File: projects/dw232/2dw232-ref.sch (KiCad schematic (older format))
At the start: 24 parts, among them P501 CONN_01X07, Q501 MMBT3904, Q502 MMBT3904, U501 LM741, U502 LM741, U503 2DW232

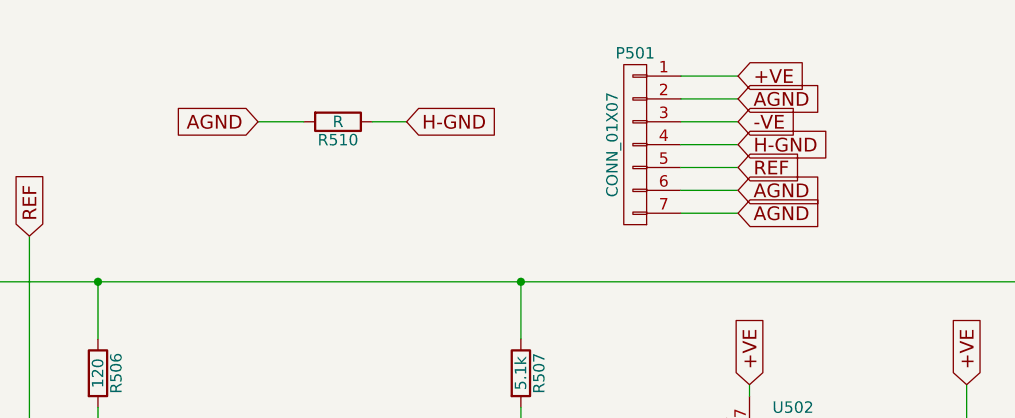
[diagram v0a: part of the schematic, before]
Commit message: remove old stuff for reference
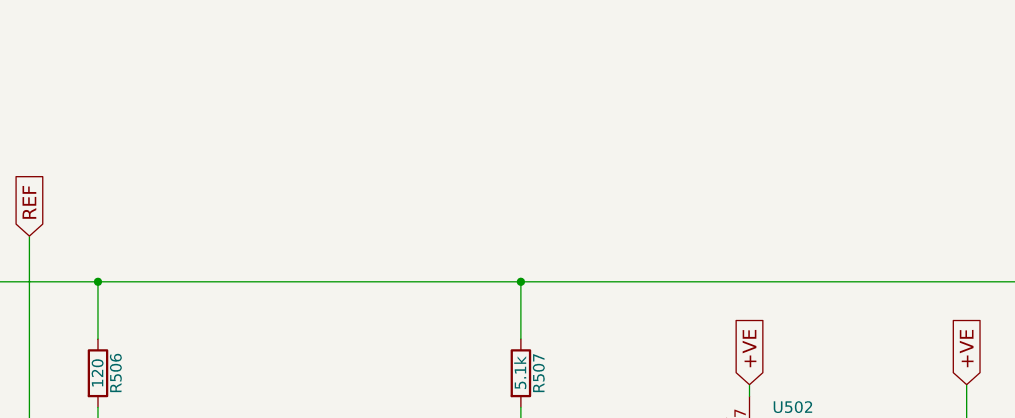
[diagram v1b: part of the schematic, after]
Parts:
- removed P501: CONN_01X07, Pin_Headers:Pin_Header_Straight_1x07, symbol CONN_01X07
- removed R510: R, Resistors_SMD:R_1206, symbol R
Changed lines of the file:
@@
 $Descr A4 11693 8268
 encoding utf-8
-Sheet 2 4
+Sheet 2 2
 Title ""
 Date ""
@@
 	1850 1400 1850 1600
 $Comp
-L CONN_01X07 P501
-U 1 1 5883052B
-P 6800 1150
-F 0 "P501" H 6800 1550 50  0000 C CNN
-F 1 "CONN_01X07" V 6900 1150 50  0000 C CNN
-F 2 "Pin_Headers:Pin_Header_Straight_1x07" H 6800 1150 50  0001 C CNN
-F 3 "" H 6800 1150 50  0000 C CNN
-	1    6800 1150
-	-1   0    0    -1
-$EndComp
-Text GLabel 7250 850  2    60   Input ~ 0
-+VE
-Wire Wire Line
-	7000 850  7250 850
-Text GLabel 7250 950  2    60   Input ~ 0
-AGND
-Wire Wire Line
-	7000 950  7250 950
-Text GLabel 7250 1250 2    60   Input ~ 0
-REF
-Text GLabel 7250 1350 2    60   Input ~ 0
-AGND
-Text GLabel 7250 1450 2    60   Input ~ 0
-AGND
-Wire Wire Line
-	7000 1350 7250 1350
-Wire Wire Line
-	7000 1450 7250 1450
-$Comp
 L MMBT3904 Q502
 U 1 1 58835E41
@@
 Text GLabel 5850 2900 2    60   Input ~ 0
 H-GND
-Text GLabel 7250 1050 2    60   Input ~ 0
--VE
-Wire Wire Line
-	7000 1050 7250 1050
-Text GLabel 7250 1150 2    60   Input ~ 0
-H-GND
-Wire Wire Line
-	7000 1150 7250 1150
-Wire Wire Line
-	7000 1250 7250 1250
 Text GLabel 2600 4050 3    60   Input ~ 0
 -VE
@@
 Wire Wire Line
 	7300 2850 7300 3000
-Text GLabel 5800 1050 2    60   Input ~ 0
-H-GND
-Text GLabel 5150 1050 0    60   Input ~ 0
-AGND
-$Comp
-L R R510
-U 1 1 5883C0FE
-P 5500 1050
-F 0 "R510" V 5580 1050 50  0000 C CNN
-F 1 "R" V 5500 1050 50  0000 C CNN
-F 2 "Resistors_SMD:R_1206" V 5430 1050 50  0001 C CNN
-F 3 "" H 5500 1050 50  0000 C CNN
-	1    5500 1050
-	0    1    1    0
-$EndComp
-Wire Wire Line
-	5150 1050 5350 1050
-Wire Wire Line
-	5650 1050 5800 1050
 $Comp
 L 2DW232 U503

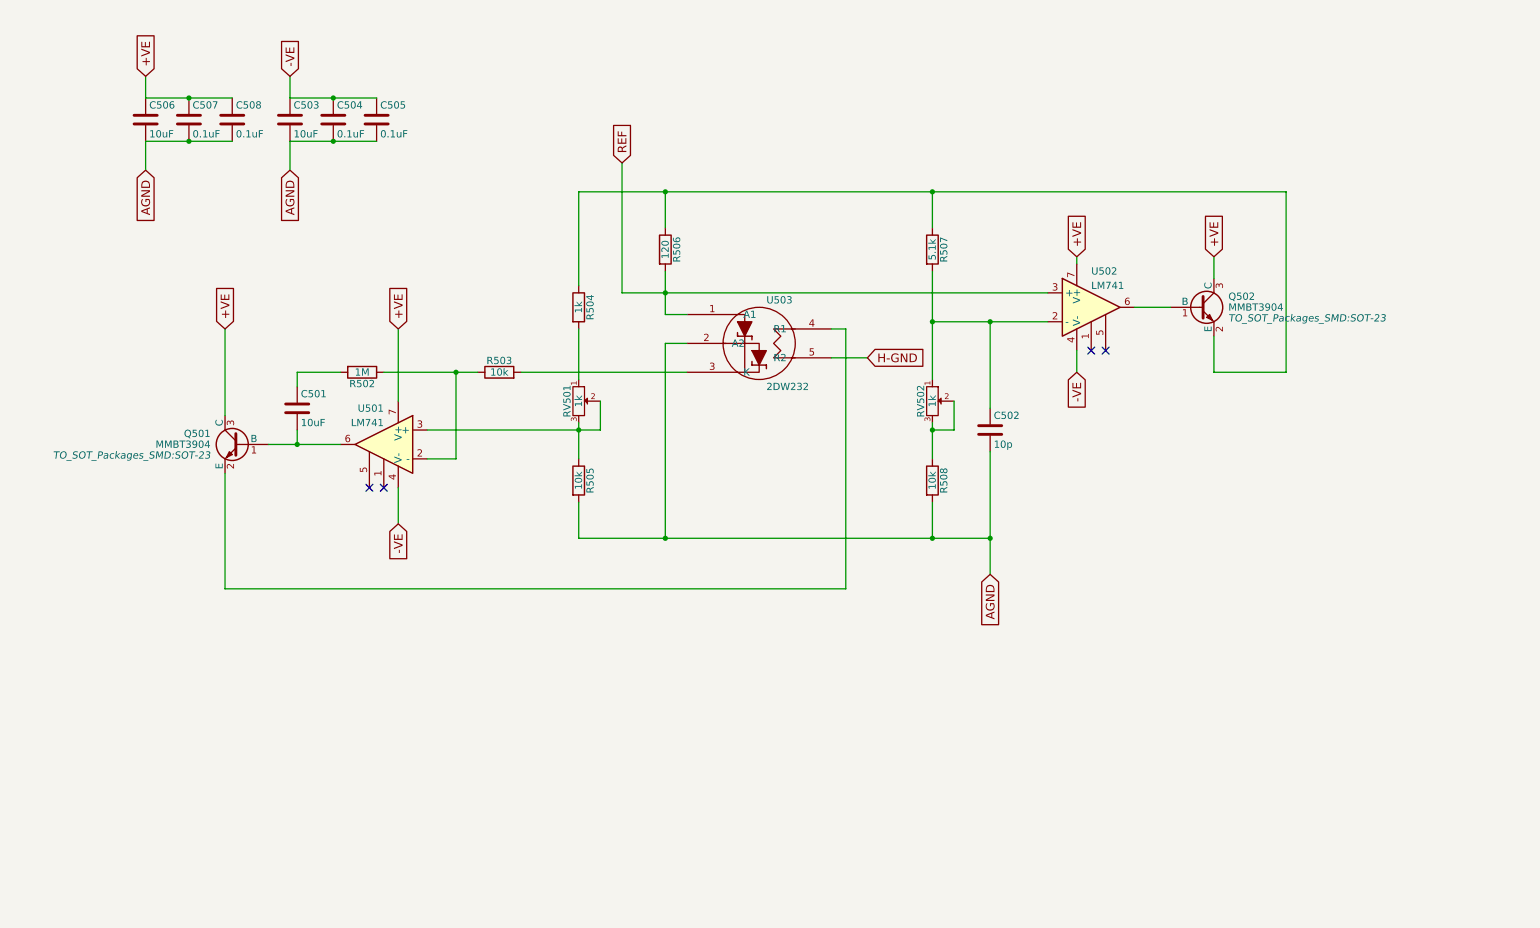
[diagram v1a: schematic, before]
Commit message: change trimmers to fixed resistors
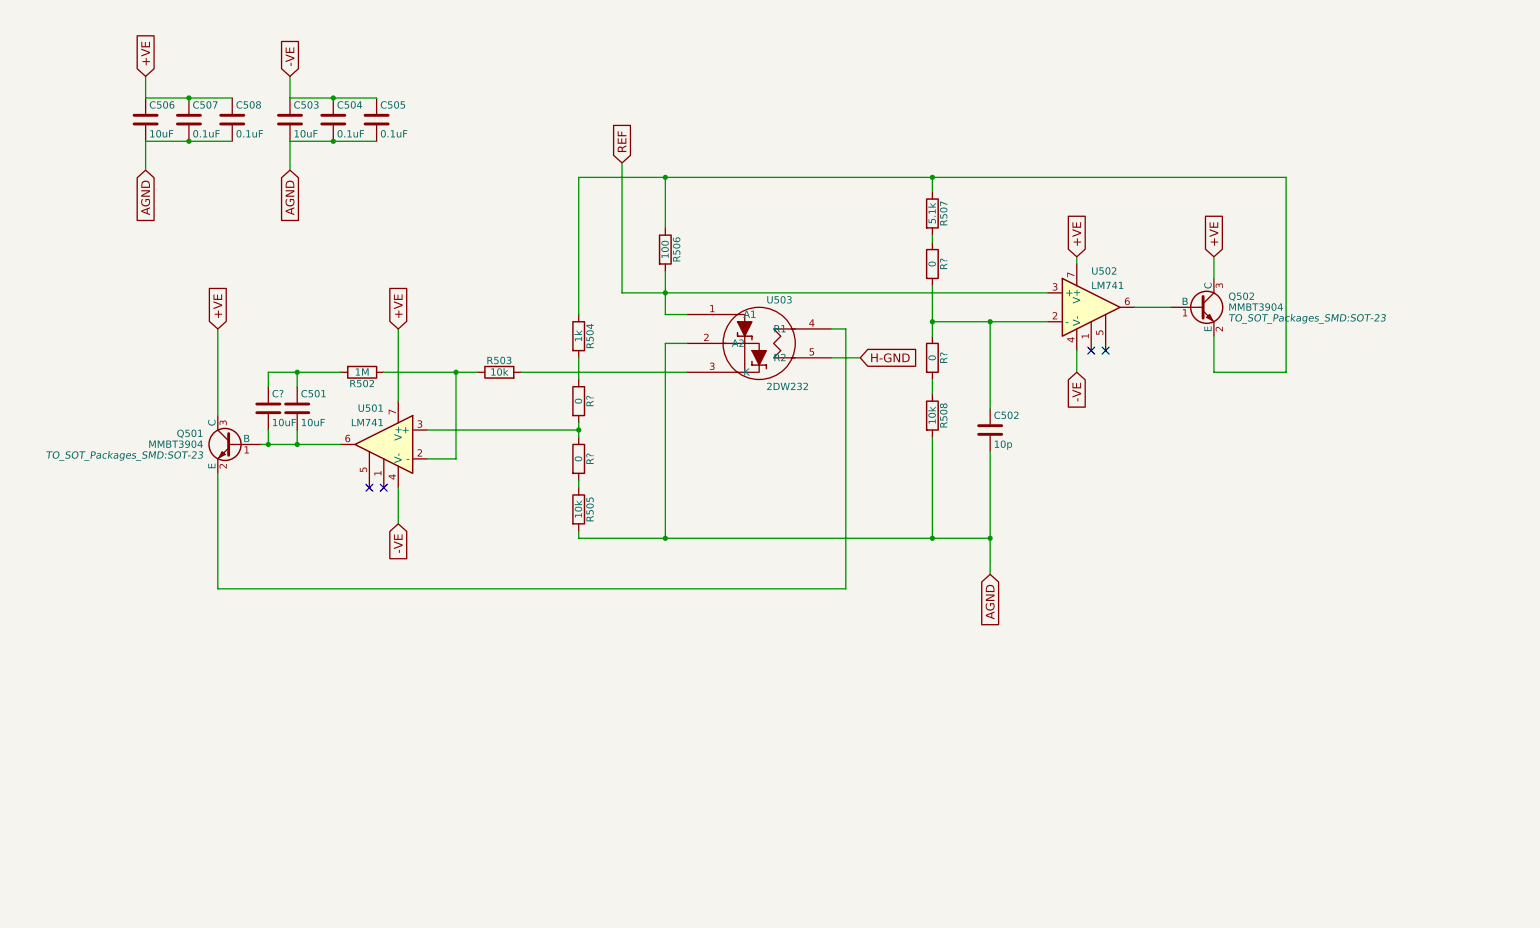
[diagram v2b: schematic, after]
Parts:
- removed RV501, RV502: 1k, Potentiometers:Potentiometer_Bourns_3296Y_3-8Zoll_Angular_ScrewUp, symbol POT
- added C?: 10uF, Capacitors_SMD:C_1206, symbol C
- added R? (x4): 0, Resistors_ThroughHole:Resistor_TO-220_Vertical, symbol R
- R506: value 120 -> 100
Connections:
- net at C502.1, U502.2 (-): now also R?.1, R?.2; no longer R507.2
- net at R508.1: now also R?.2
- net at R504.2: now also R?.1
- net at R505.1: now also R?.2; no longer U501.3 (+)
- net at C501.2, Q501.1 (B), U501.6: now also C?.2
- net at C501.1, R502.2: now also C?.1
- new net: R507.2, R?.1
- new net: R?.1, R?.2, U501.3 (+)
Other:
- moved on the sheet: Q501, R504, R505, R507, R508
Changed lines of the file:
@@
 L R R508
 U 1 1 5881849D
-P 6300 3750
-F 0 "R508" V 6380 3750 50  0000 C CNN
-F 1 "10k" V 6300 3750 50  0000 C CNN
-F 2 "Resistors_ThroughHole:Resistor_TO-220_Vertical" V 6230 3750 50  0001 C CNN
-F 3 "" H 6300 3750 50  0000 C CNN
-	1    6300 3750
+P 6300 3300
+F 0 "R508" V 6380 3300 50  0000 C CNN
+F 1 "10k" V 6300 3300 50  0000 C CNN
+F 2 "Resistors_ThroughHole:Resistor_TO-220_Vertical" V 6230 3300 50  0001 C CNN
+F 3 "" H 6300 3300 50  0000 C CNN
+	1    6300 3300
 	1    0    0    -1
 $EndComp
@@
 L R R507
 U 1 1 588184DE
-P 6300 2150
-F 0 "R507" V 6380 2150 50  0000 C CNN
-F 1 "5.1k" V 6300 2150 50  0000 C CNN
-F 2 "Resistors_ThroughHole:Resistor_TO-220_Vertical" V 6230 2150 50  0001 C CNN
-F 3 "" H 6300 2150 50  0000 C CNN
-	1    6300 2150
-	1    0    0    -1
-$EndComp
-Wire Wire Line
-	3850 1750 8750 1750
-Wire Wire Line
-	6300 1750 6300 2000
-Wire Wire Line
-	6300 2300 6300 3050
+P 6300 1900
+F 0 "R507" V 6380 1900 50  0000 C CNN
+F 1 "5.1k" V 6300 1900 50  0000 C CNN
+F 2 "Resistors_ThroughHole:Resistor_TO-220_Vertical" V 6230 1900 50  0001 C CNN
+F 3 "" H 6300 1900 50  0000 C CNN
+	1    6300 1900
+	1    0    0    -1
+$EndComp
+Wire Wire Line
+	3850 1650 8750 1650
+Wire Wire Line
+	6300 1650 6300 1750
+Wire Wire Line
+	6300 2400 6300 2750
 Text GLabel 7300 2200 1    60   Input ~ 0
 +VE
@@
 P 4450 2150
 F 0 "R506" V 4530 2150 50  0000 C CNN
-F 1 "120" V 4450 2150 50  0000 C CNN
+F 1 "100" V 4450 2150 50  0000 C CNN
 F 2 "Resistors_ThroughHole:Resistor_TO-220_Vertical" V 4380 2150 50  0001 C CNN
 F 3 "" H 4450 2150 50  0000 C CNN
@@
 	1    0    0    -1
 $EndComp
-Connection ~ 6300 1750
+Connection ~ 6300 1650
 Text GLabel 8250 2200 1    60   Input ~ 0
 +VE
@@
 L R R504
 U 1 1 58819A67
-P 3850 2550
-F 0 "R504" V 3930 2550 50  0000 C CNN
-F 1 "1k" V 3850 2550 50  0000 C CNN
-F 2 "Resistors_ThroughHole:Resistor_TO-220_Vertical" V 3780 2550 50  0001 C CNN
-F 3 "" H 3850 2550 50  0000 C CNN
-	1    3850 2550
-	1    0    0    -1
-$EndComp
-Wire Wire Line
-	3850 1750 3850 2400
-$Comp
-L POT RV501
-U 1 1 58819ACE
-P 3850 3200
-F 0 "RV501" H 3850 3120 50  0000 C CNN
-F 1 "1k" H 3850 3200 50  0000 C CNN
-F 2 "Potentiometers:Potentiometer_Bourns_3296Y_3-8Zoll_Angular_ScrewUp" H 3850 3200 50  0001 C CNN
-F 3 "" H 3850 3200 50  0000 C CNN
-	1    3850 3200
-	0    1    1    0
-$EndComp
+P 3850 2750
+F 0 "R504" V 3930 2750 50  0000 C CNN
+F 1 "1k" V 3850 2750 50  0000 C CNN
+F 2 "Resistors_ThroughHole:Resistor_TO-220_Vertical" V 3780 2750 50  0001 C CNN
+F 3 "" H 3850 2750 50  0000 C CNN
+	1    3850 2750
+	1    0    0    -1
+$EndComp
+Wire Wire Line
+	3850 1650 3850 2600
 $Comp
 L R R505
 U 1 1 58819B03
-P 3850 3750
-F 0 "R505" V 3930 3750 50  0000 C CNN
-F 1 "10k" V 3850 3750 50  0000 C CNN
-F 2 "Resistors_ThroughHole:Resistor_TO-220_Vertical" V 3780 3750 50  0001 C CNN
-F 3 "" H 3850 3750 50  0000 C CNN
-	1    3850 3750
-	1    0    0    -1
-$EndComp
-Wire Wire Line
-	3850 2700 3850 3050
-Wire Wire Line
-	3850 3350 3850 3600
-Wire Wire Line
-	2800 3400 4000 3400
+P 3850 3950
+F 0 "R505" V 3930 3950 50  0000 C CNN
+F 1 "10k" V 3850 3950 50  0000 C CNN
+F 2 "Resistors_ThroughHole:Resistor_TO-220_Vertical" V 3780 3950 50  0001 C CNN
+F 3 "" H 3850 3950 50  0000 C CNN
+	1    3850 3950
+	1    0    0    -1
+$EndComp
+Wire Wire Line
+	3850 2900 3850 3050
 Connection ~ 3850 3400
-Wire Wire Line
-	4000 3400 4000 3200
 $Comp
 L LM741 U501
@@
 $EndComp
 Wire Wire Line
-	2200 3000 1900 3000
+	1700 3000 2200 3000
 Wire Wire Line
 	1900 3000 1900 3100
@@
 	1900 3400 1900 3500
 Wire Wire Line
-	1700 3500 2200 3500
+	1650 3500 2200 3500
 Text GLabel 2600 2700 1    60   Input ~ 0
 +VE
@@
 	2600 2700 2600 3200
 Connection ~ 1900 3500
-Text GLabel 1400 2700 1    60   Input ~ 0
+Text GLabel 1350 2700 1    60   Input ~ 0
 +VE
 Wire Wire Line
-	1400 2700 1400 3300
-Wire Wire Line
-	8750 1750 8750 3000
+	1350 2700 1350 3300
+Wire Wire Line
+	8750 1650 8750 3000
 Wire Wire Line
 	8750 3000 8250 3000
@@
 NoConn ~ 2500 3800
 Wire Wire Line
-	6300 3900 6300 4150
-Wire Wire Line
-	3850 3900 3850 4150
+	6300 3450 6300 4150
+Wire Wire Line
+	3850 4100 3850 4150
 Wire Wire Line
 	6700 3550 6700 4400
 Connection ~ 6700 4150
 Wire Wire Line
-	6300 3350 6300 3600
+	6300 3050 6300 3150
 $Comp
 L C C503
@@
 L MMBT3904 Q501
 U 1 1 58836CA2
-P 1500 3500
-F 0 "Q501" H 1700 3575 50  0000 L CNN
-F 1 "MMBT3904" H 1700 3500 50  0000 L CNN
-F 2 "TO_SOT_Packages_SMD:SOT-23" H 1700 3425 50  0000 L CIN
-F 3 "" H 1500 3500 50  0000 L CNN
-	1    1500 3500
+P 1450 3500
+F 0 "Q501" H 1650 3575 50  0000 L CNN
+F 1 "MMBT3904" H 1650 3500 50  0000 L CNN
+F 2 "TO_SOT_Packages_SMD:SOT-23" H 1650 3425 50  0000 L CIN
+F 3 "" H 1450 3500 50  0000 L CNN
+	1    1450 3500
 	-1   0    0    -1
 $EndComp
 Wire Wire Line
-	1400 3700 1400 4500
-Text GLabel 5850 2900 2    60   Input ~ 0
+	1350 3700 1350 4500
+Text GLabel 5800 2900 2    60   Input ~ 0
 H-GND
 Text GLabel 2600 4050 3    60   Input ~ 0
@@
 	4450 2300 4450 2600
 Wire Wire Line
-	4450 1750 4450 2000
-Connection ~ 4450 1750
+	4450 1650 4450 2000
+Connection ~ 4450 1650
 Connection ~ 4450 2450
 Wire Wire Line
-	1400 4500 5700 4500
+	1350 4500 5700 4500
 Wire Wire Line
 	5600 2700 5700 2700
@@
 	5700 2700 5700 4500
 Wire Wire Line
-	5600 2900 5850 2900
-$Comp
-L POT RV502
-U 1 1 588334E0
-P 6300 3200
-F 0 "RV502" H 6300 3120 50  0000 C CNN
-F 1 "1k" H 6300 3200 50  0000 C CNN
-F 2 "Potentiometers:Potentiometer_Bourns_3296Y_3-8Zoll_Angular_ScrewUp" H 6300 3200 50  0001 C CNN
-F 3 "" H 6300 3200 50  0000 C CNN
-	1    6300 3200
-	0    1    1    0
-$EndComp
-Wire Wire Line
-	6450 3200 6450 3400
-Wire Wire Line
-	6450 3400 6300 3400
-Connection ~ 6300 3400
+	5600 2900 5800 2900
 $Comp
 L C C506
@@
 Wire Wire Line
 	4150 1550 4150 2450
+$Comp
+L R R?
+U 1 1 58A3A42F
+P 3850 3600
+F 0 "R?" V 3930 3600 50  0000 C CNN
+F 1 "0" V 3850 3600 50  0000 C CNN
+F 2 "Resistors_ThroughHole:Resistor_TO-220_Vertical" V 3780 3600 50  0001 C CNN
+F 3 "" H 3850 3600 50  0000 C CNN
+	1    3850 3600
+	1    0    0    -1
+$EndComp
+Wire Wire Line
+	3850 3750 3850 3800
+Wire Wire Line
+	3850 3350 3850 3450
+Wire Wire Line
+	3850 3400 2800 3400
+$Comp
+L R R?
+U 1 1 58A3A676
+P 3850 3200
+F 0 "R?" V 3930 3200 50  0000 C CNN
+F 1 "0" V 3850 3200 50  0000 C CNN
+F 2 "Resistors_ThroughHole:Resistor_TO-220_Vertical" V 3780 3200 50  0001 C CNN
+F 3 "" H 3850 3200 50  0000 C CNN
+	1    3850 3200
+	1    0    0    -1
+$EndComp
+$Comp
+L R R?
+U 1 1 58A3AFA3
+P 6300 2900
+F 0 "R?" V 6380 2900 50  0000 C CNN
+F 1 "0" V 6300 2900 50  0000 C CNN
+F 2 "Resistors_ThroughHole:Resistor_TO-220_Vertical" V 6230 2900 50  0001 C CNN
+F 3 "" H 6300 2900 50  0000 C CNN
+	1    6300 2900
+	1    0    0    -1
+$EndComp
+$Comp
+L R R?
+U 1 1 58A3B1B3
+P 6300 2250
+F 0 "R?" V 6380 2250 50  0000 C CNN
+F 1 "0" V 6300 2250 50  0000 C CNN
+F 2 "Resistors_ThroughHole:Resistor_TO-220_Vertical" V 6230 2250 50  0001 C CNN
+F 3 "" H 6300 2250 50  0000 C CNN
+	1    6300 2250
+	1    0    0    -1
+$EndComp
+Wire Wire Line
+	6300 2050 6300 2100
+$Comp
+L C C?
+U 1 1 58A3D583
+P 1700 3250
+F 0 "C?" H 1725 3350 50  0000 L CNN
+F 1 "10uF" H 1725 3150 50  0000 L CNN
+F 2 "Capacitors_SMD:C_1206" H 1738 3100 50  0001 C CNN
+F 3 "" H 1700 3250 50  0000 C CNN
+	1    1700 3250
+	1    0    0    -1
+$EndComp
+Wire Wire Line
+	1700 3000 1700 3100
+Connection ~ 1900 3000
+Wire Wire Line
+	1700 3400 1700 3500
+Connection ~ 1700 3500
 $EndSCHEMATC
